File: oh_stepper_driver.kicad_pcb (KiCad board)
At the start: 2 copper layers, 61 x 43.2 mm, 33 parts, among them P1 CONN_01X04, P2 CONN_01X02, P3 CONN_01X02, Q1 CSD18531Q5A, Q2 CSD18531Q5A, Q3 CSD18531Q5A, Q4 CSD18531Q5A, Q5 CSD18531Q5A, Q6 CSD18531Q5A, Q7 CSD18531Q5A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

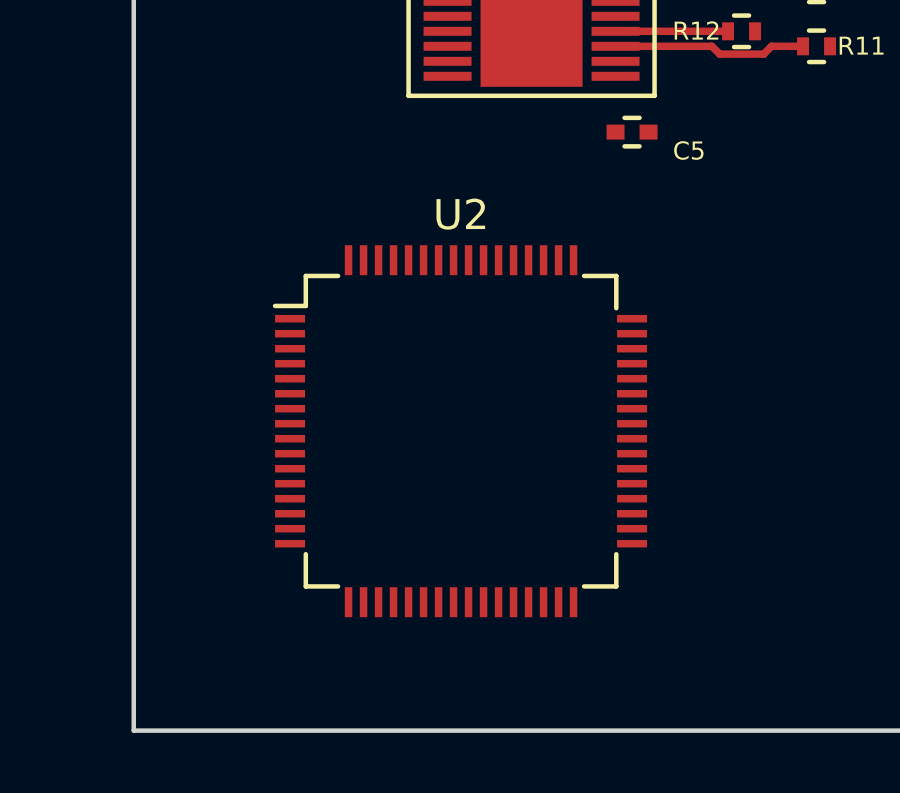
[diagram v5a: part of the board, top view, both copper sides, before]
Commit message: connecting control lines between the motor driver and the STM32
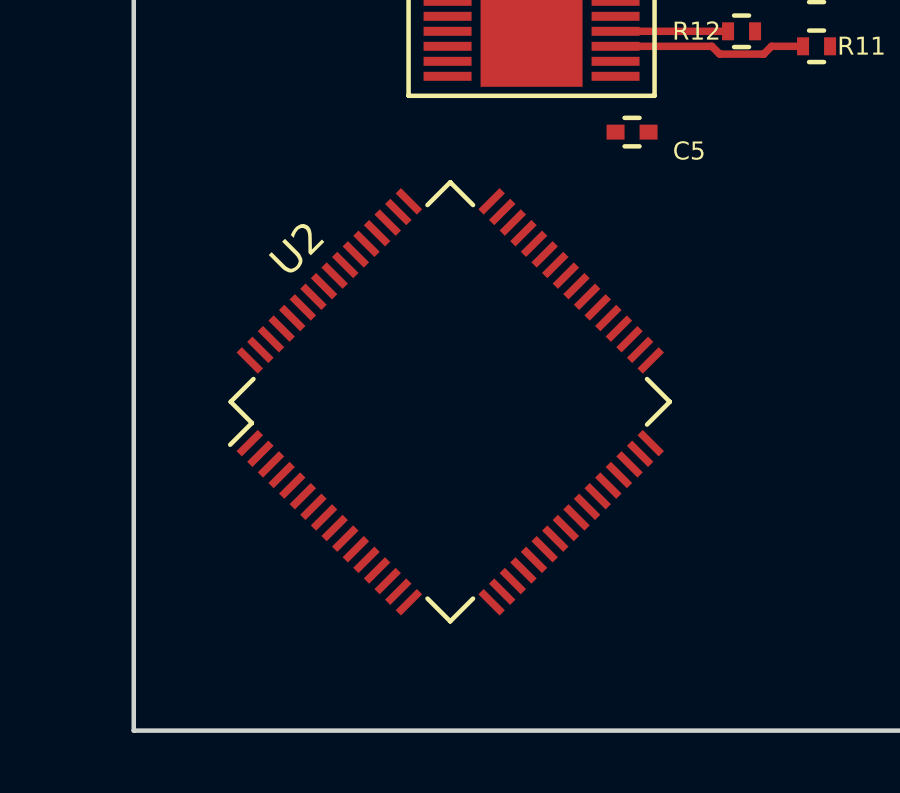
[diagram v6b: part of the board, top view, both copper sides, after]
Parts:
- moved U2 1.04 mm to (127.4, 88.1), turned to 45 degrees
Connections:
- U2 pad 49: Net-(U2-Pad49) -> /STALLn
- U2 pad 50: Net-(U2-Pad50) -> /FAULTn
- U2 pad 51: Net-(U2-Pad51) -> /SDATAO
- U2 pad 52: Net-(U2-Pad52) -> /SCS
- U2 pad 53: Net-(U2-Pad53) -> /SDATI
- U2 pad 54: Net-(U2-Pad54) -> /SCLK
- U2 pad 55: Net-(U2-Pad55) -> /BIN2
- U2 pad 56: Net-(U2-Pad56) -> /BIN1
- U2 pad 57: Net-(U2-Pad57) -> /DIR_AIN2
- U2 pad 58: Net-(U2-Pad58) -> /STEP_AIN1
- U2 pad 59: Net-(U2-Pad59) -> /RESET
- U2 pad 61: Net-(U2-Pad61) -> /SLEEPn

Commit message: connecting mcu
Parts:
- moved C1 4.21 mm to (123.8, 65.5)
- moved C2 4.21 mm to (123.8, 64.0)
- moved C3 4.21 mm to (123.8, 62.0)
- moved C4 4.21 mm to (123.8, 67.0)
- moved C5 4.21 mm to (133.7, 74.9)
- moved R10 4.21 mm to (139.8, 70.0)
- moved R11 4.21 mm to (139.8, 72.0)
- moved R12 4.21 mm to (137.3, 71.5)
- moved R3 4.21 mm to (137.3, 65.0)
- moved R4 4.21 mm to (139.8, 65.5)
- moved R5 4.21 mm to (139.8, 67.5)
- moved R6 4.21 mm to (137.3, 67.0)
- moved R9 4.21 mm to (137.3, 69.5)
- moved U1 4.21 mm to (130.3, 68.5)
- moved U2 1.08 mm to (128.3, 88.6), turned to 90 degrees
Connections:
- net Net-(U2-Pad46) renamed /JTMS
- U2 pad 1: Net-(U2-Pad1) -> +3V3
- U2 pad 21: Net-(U2-Pad21) -> /STALLn
- U2 pad 22: Net-(U2-Pad22) -> /FAULTn
- U2 pad 23: Net-(U2-Pad23) -> /BIN2
- U2 pad 41: Net-(U2-Pad41) -> /BIN1
- U2 pad 42: Net-(U2-Pad42) -> /DIR_AIN2
- U2 pad 43: Net-(U2-Pad43) -> /STEP_AIN1
- U2 pad 44: Net-(U2-Pad44) -> /RESET
- U2 pad 45: Net-(U2-Pad45) -> /SLEEPn
- U2 pad 49: /STALLn -> /JTCK
- U2 pad 50: /FAULTn -> /JTDI
- U2 pad 55: /BIN2 -> /JTDO
- U2 pad 56: /BIN1 -> /NJTRST
- U2 pad 57: /DIR_AIN2 -> Net-(U2-Pad57)
- U2 pad 58: /STEP_AIN1 -> Net-(U2-Pad58)
- U2 pad 59: /RESET -> Net-(U2-Pad59)
- U2 pad 61: /SLEEPn -> Net-(U2-Pad61)

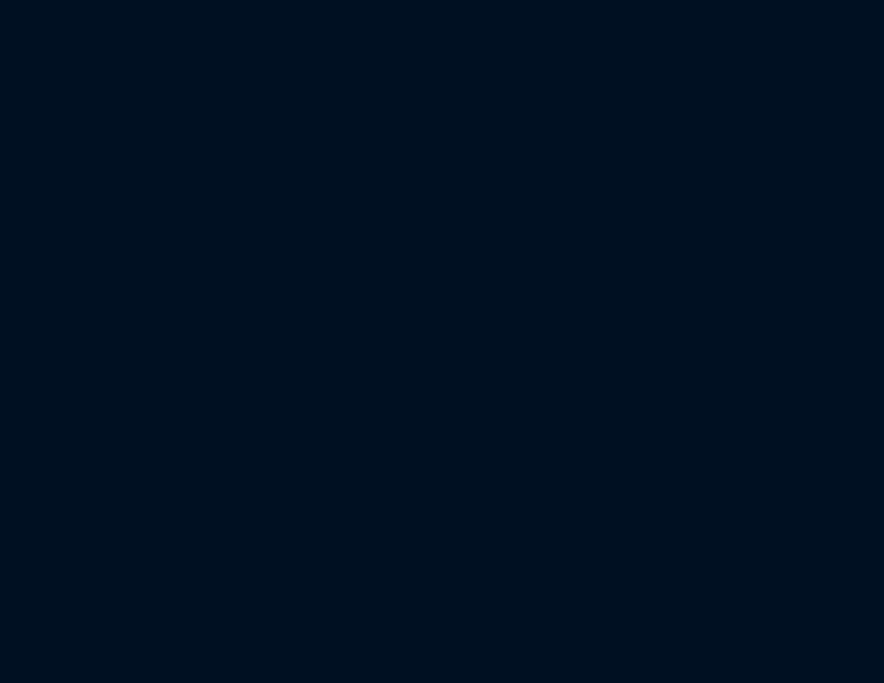
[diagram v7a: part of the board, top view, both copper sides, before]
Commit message: fp-lib-table fixed
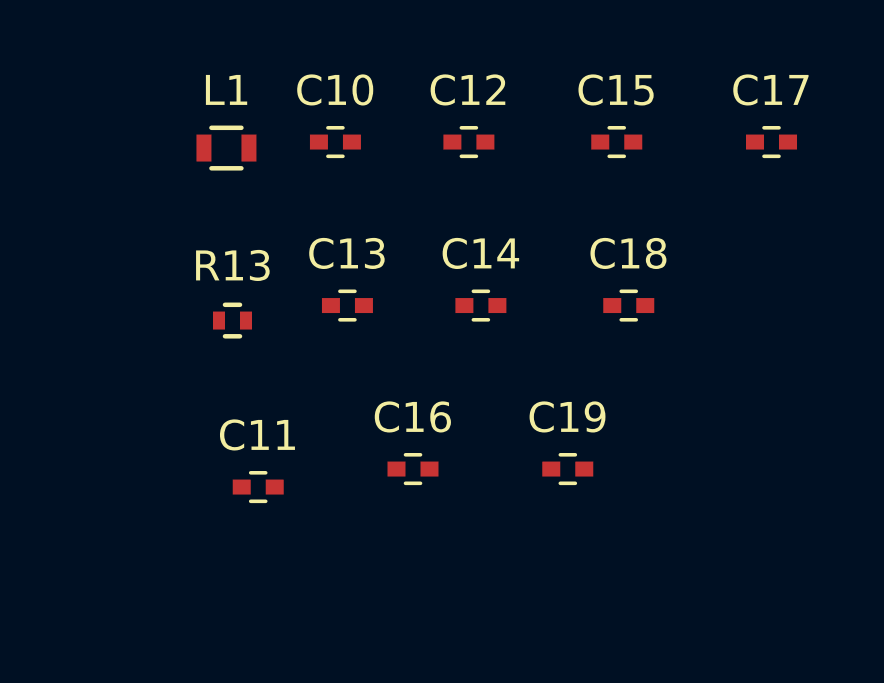
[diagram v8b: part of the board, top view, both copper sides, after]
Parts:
- added C10: 10pF, Capacitors_SMD:C_0402, F.Cu at (223.3, 58.5)
- added C11: 100nF, Capacitors_SMD:C_0402, F.Cu at (220.7, 70.0)
- added C12: 2.2uF, Capacitors_SMD:C_0402, F.Cu at (227.8, 58.5)
- added C13: 10pF, Capacitors_SMD:C_0402, F.Cu at (223.7, 63.9)
- added C14: 2.2uF, Capacitors_SMD:C_0402, F.Cu at (228.2, 63.9)
- added C15: 100nF, Capacitors_SMD:C_0402, F.Cu at (232.7, 58.5)
- added C16: 100nF, Capacitors_SMD:C_0402, F.Cu at (225.9, 69.4)
- added C17: 100nF, Capacitors_SMD:C_0402, F.Cu at (237.8, 58.5)
- added C18: 100nF, Capacitors_SMD:C_0402, F.Cu at (233.1, 63.9)
- added C19: 100nF, Capacitors_SMD:C_0402, F.Cu at (231.1, 69.4)
- added L1: FB, Resistors_SMD:R_0603, F.Cu at (219.7, 58.7)
- added R13: 10k, Resistors_SMD:R_0402, F.Cu at (219.9, 64.4)
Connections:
- U2 pad 10: Net-(U2-Pad10) -> (no net)
- U2 pad 11: Net-(U2-Pad11) -> (no net)
- U2 pad 14: Net-(U2-Pad14) -> (no net)
- U2 pad 15: Net-(U2-Pad15) -> (no net)
- U2 pad 16: Net-(U2-Pad16) -> (no net)
- U2 pad 17: Net-(U2-Pad17) -> (no net)
- U2 pad 2: Net-(U2-Pad2) -> (no net)
- U2 pad 20: Net-(U2-Pad20) -> (no net)
- U2 pad 24: Net-(U2-Pad24) -> (no net)
- U2 pad 25: Net-(U2-Pad25) -> (no net)
- U2 pad 26: Net-(U2-Pad26) -> (no net)
- U2 pad 27: Net-(U2-Pad27) -> (no net)
- U2 pad 28: Net-(U2-Pad28) -> (no net)
- U2 pad 29: Net-(U2-Pad29) -> (no net)
- U2 pad 3: Net-(U2-Pad3) -> (no net)
- U2 pad 30: Net-(U2-Pad30) -> (no net)
- U2 pad 33: Net-(U2-Pad33) -> (no net)
- U2 pad 34: Net-(U2-Pad34) -> (no net)
- U2 pad 35: Net-(U2-Pad35) -> (no net)
- U2 pad 36: Net-(U2-Pad36) -> (no net)
- U2 pad 37: Net-(U2-Pad37) -> (no net)
- U2 pad 38: Net-(U2-Pad38) -> (no net)
- U2 pad 39: Net-(U2-Pad39) -> (no net)
- U2 pad 4: Net-(U2-Pad4) -> (no net)
- U2 pad 40: Net-(U2-Pad40) -> (no net)
- U2 pad 46: /JTMS -> (no net)
- U2 pad 49: /JTCK -> (no net)
- U2 pad 50: /JTDI -> (no net)
- U2 pad 55: /JTDO -> (no net)
- U2 pad 56: /NJTRST -> (no net)
- U2 pad 57: Net-(U2-Pad57) -> (no net)
- U2 pad 58: Net-(U2-Pad58) -> (no net)
- U2 pad 59: Net-(U2-Pad59) -> (no net)
- U2 pad 61: Net-(U2-Pad61) -> (no net)
- U2 pad 62: Net-(U2-Pad62) -> (no net)
- U2 pad 8: Net-(U2-Pad8) -> (no net)
- U2 pad 9: Net-(U2-Pad9) -> (no net)
